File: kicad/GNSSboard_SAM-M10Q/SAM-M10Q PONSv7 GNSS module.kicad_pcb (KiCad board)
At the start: 2 copper layers, 52 x 86 mm, 6 parts, among them J2 Conn_01x05, U2 SAM-M10Q-00B

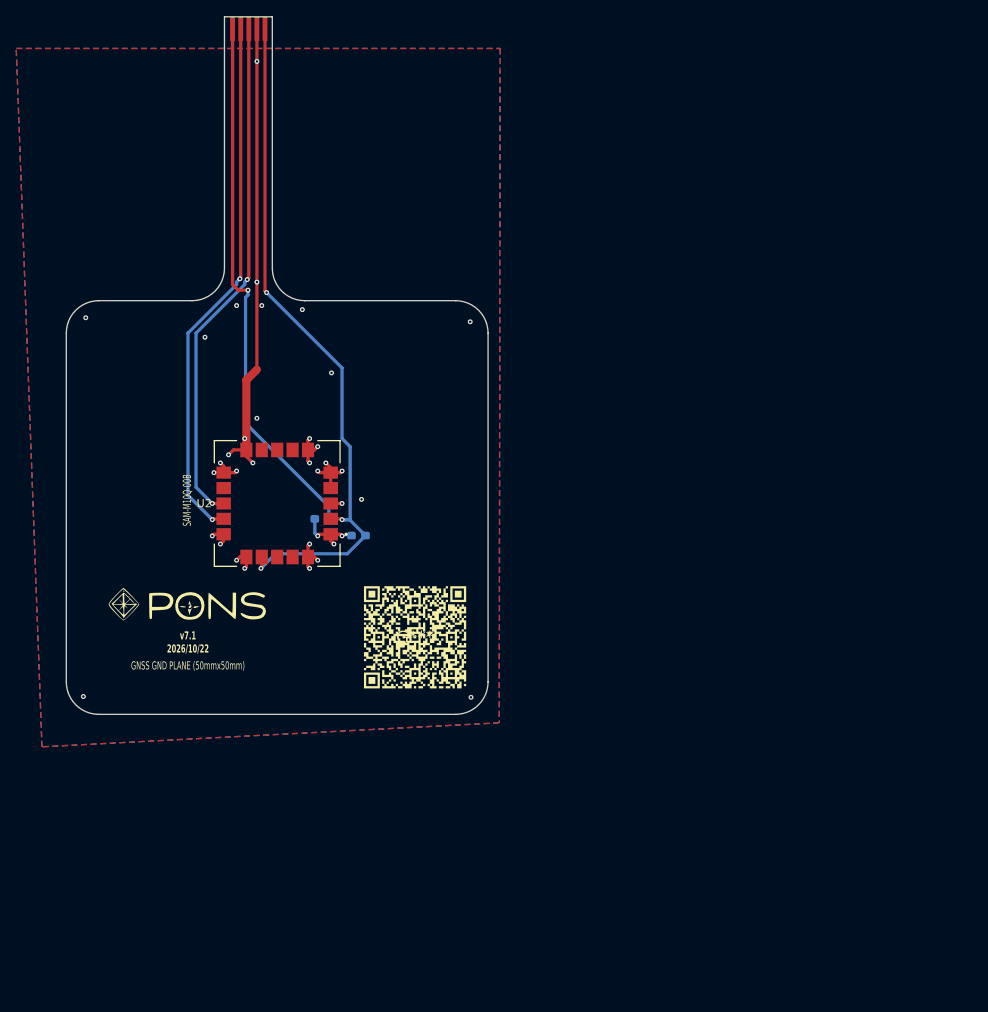
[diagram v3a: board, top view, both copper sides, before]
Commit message: 0.995 無線で化けたフレームを数え直していたのを直し、仮の音声 5 つを録音に差し替え、画面のセンサー名を基板に合わせ、起動ロゴを生成ツールで焼くようにし、README を v7.1 の発注方法に書き直した
Co-Authored-By: Claude Opus 5.5 <noreply@anthropic.com>
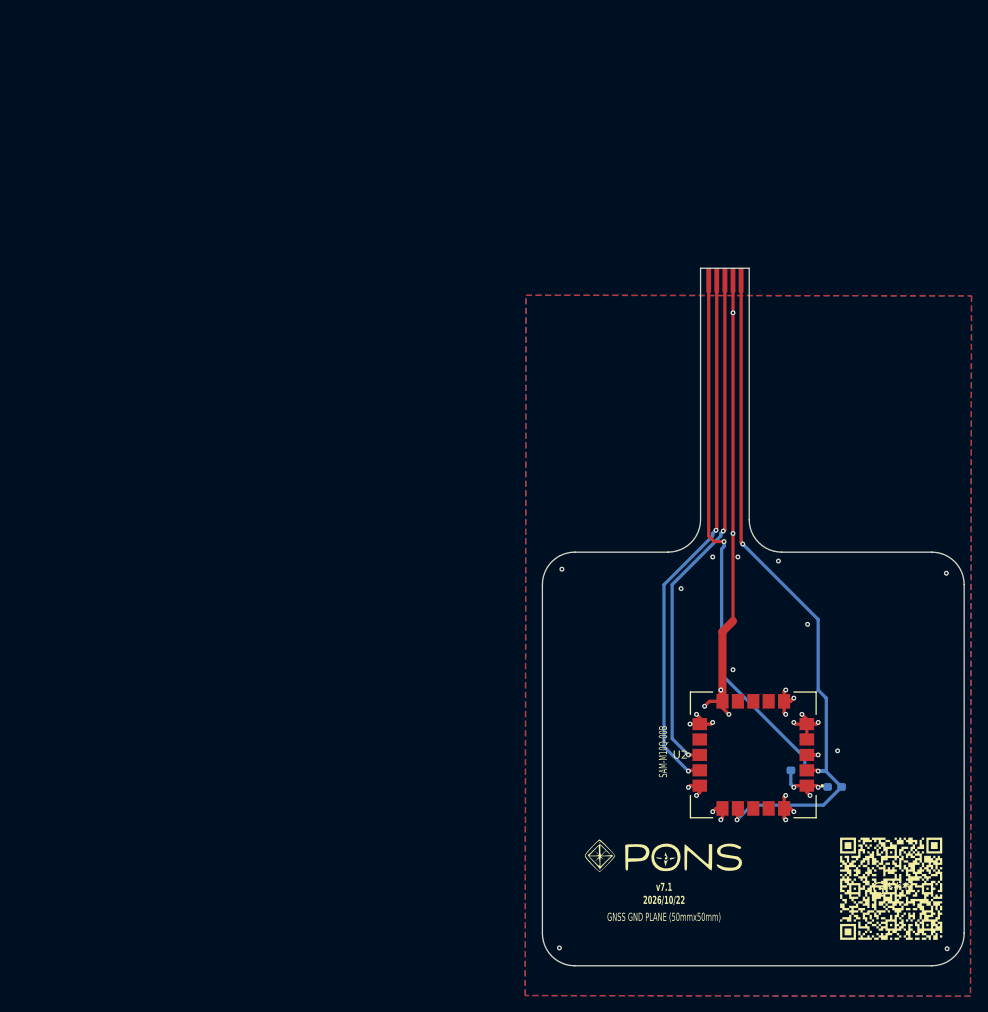
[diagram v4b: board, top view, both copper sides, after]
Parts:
- moved C2 66.4 mm to (152.7, 112.0)
- moved C3 66.4 mm to (148.2, 109.9)
- moved G*** 66.4 mm to (159.7, 124.5)
- moved G*** 66.4 mm to (131.7, 120.5)
- moved J2 66.4 mm to (139.2, 49.5)
- moved U2 66.4 mm to (142.7, 108.0)
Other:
- outline, holes or cut-outs redrawn
- board text added: "Purchase SAM-M10Q at digikey"
- board text added: "Stiffener 1/2: At Gold finger Total thickness approx. 0.3mm to 0.4mm PI Backside"
- board text added: "Stiffener 2/2: At GND plate. Total thickness approx. 0.3mm to 0.4mm PI Backside"
- board text removed: "SAM-M10Q 0.1uF x2 Resistor x2 MS621FE x1"
- board text removed: "Stiffener 1/2: At Gold finger Total thickness 0.3mm PI Backside"
- board text removed: "Stiffener 2/2: At GND plate. Total thickness 0.3mm PI Backside"
